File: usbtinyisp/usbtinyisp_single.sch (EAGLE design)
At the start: 23 parts, among them IC1 ATTINY2313-20P, IC2 74LVX125D, Q1 12000

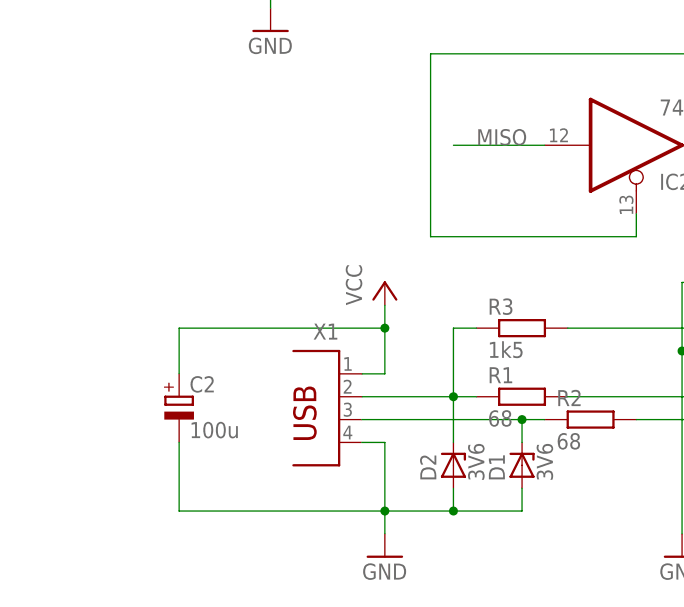
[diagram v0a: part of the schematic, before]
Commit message: add fuse and diode and route again the whole board
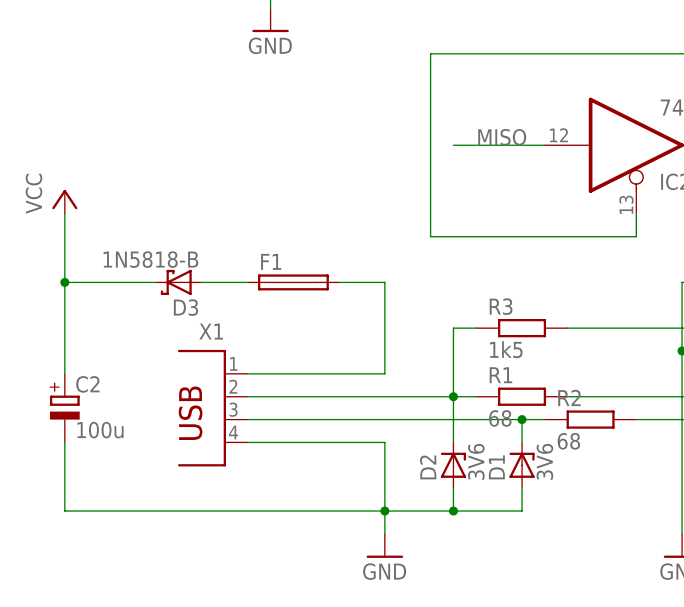
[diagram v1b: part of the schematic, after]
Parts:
- added D3: 1N5818-B, diode:1N5817-B
- added F1: (no value), n39:PTC-FUSE-LP60-050
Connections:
- new net N$14: D3.A, F1.1
- new net VBUS: F1.2, X1.1
- net VCC: now also D3.C; no longer X1.1
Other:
- moved on the sheet: C2, X1
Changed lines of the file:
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@@
 <part name="C4" library="rcl" deviceset="C-EU" device="C1206" value="22p"/>
 <part name="C5" library="rcl" deviceset="C-EU" device="C0805" value="100n"/>
+<part name="F1" library="n39" deviceset="PTC-FUSE" device="-LP60-050"/>
+<part name="D3" library="diode" deviceset="1N581*" device="" technology="7-B" value="1N5818-B"/>
 </parts>
 <sheets>
@@
 <instance part="JP3" gate="G$1" x="20.32" y="154.94" rot="MR180"/>
 <instance part="C1" gate="G$1" x="152.4" y="86.36"/>
-<instance part="P+1" gate="VCC" x="25.4" y="91.44"/>
+<instance part="P+1" gate="VCC" x="-10.16" y="101.6"/>
 <instance part="LED1" gate="G$1" x="66.04" y="91.44" rot="R270"/>
 <instance part="R6" gate="G$1" x="76.2" y="91.44"/>
@@
 <instance part="LED2" gate="G$1" x="66.04" y="83.82" rot="R270"/>
 <instance part="JP1" gate="1" x="22.86" y="134.62" rot="MR180"/>
-<instance part="X1" gate="G$1" x="20.32" y="76.2" rot="MR0"/>
+<instance part="X1" gate="G$1" x="7.62" y="76.2" rot="MR0"/>
 <instance part="IC2" gate="B" x="114.3" y="129.54" rot="R180"/>
 <instance part="IC2" gate="A" x="114.3" y="147.32" rot="R180"/>
@@
 <instance part="IC2" gate="D" x="53.34" y="106.68" rot="MR180"/>
 <instance part="IC2" gate="P" x="55.88" y="134.62"/>
-<instance part="C2" gate="G$1" x="2.54" y="78.74"/>
+<instance part="C2" gate="G$1" x="-10.16" y="78.74"/>
 <instance part="Q1" gate="G$1" x="165.1" y="99.06" rot="R90"/>
 <instance part="C3" gate="G$1" x="170.18" y="104.14" rot="R90"/>
 <instance part="C4" gate="G$1" x="170.18" y="93.98" rot="R90"/>
 <instance part="C5" gate="G$1" x="45.72" y="134.62"/>
+<instance part="F1" gate="G$1" x="15.24" y="91.44"/>
+<instance part="D3" gate="G$1" x="2.54" y="91.44" rot="R180"/>
 </instances>
 <busses>
@@
 <net name="N$1" class="0">
 <segment>
-<wire x1="22.86" y1="78.74" x2="33.02" y2="78.74" width="0.1524" layer="91"/>
+<wire x1="10.16" y1="78.74" x2="33.02" y2="78.74" width="0.1524" layer="91"/>
 <wire x1="33.02" y1="78.74" x2="35.56" y2="78.74" width="0.1524" layer="91"/>
 <wire x1="35.56" y1="86.36" x2="33.02" y2="86.36" width="0.1524" layer="91"/>
@@
 <net name="N$2" class="0">
 <segment>
-<wire x1="22.86" y1="76.2" x2="40.64" y2="76.2" width="0.1524" layer="91"/>
+<wire x1="10.16" y1="76.2" x2="40.64" y2="76.2" width="0.1524" layer="91"/>
 <wire x1="43.18" y1="76.2" x2="40.64" y2="76.2" width="0.1524" layer="91"/>
 <wire x1="40.64" y1="76.2" x2="40.64" y2="73.66" width="0.1524" layer="91"/>
@@
 </segment>
 <segment>
-<wire x1="25.4" y1="88.9" x2="25.4" y2="86.36" width="0.1524" layer="91"/>
-<wire x1="25.4" y1="86.36" x2="25.4" y2="81.28" width="0.1524" layer="91"/>
-<wire x1="25.4" y1="81.28" x2="22.86" y2="81.28" width="0.1524" layer="91"/>
-<wire x1="25.4" y1="86.36" x2="2.54" y2="86.36" width="0.1524" layer="91"/>
-<wire x1="2.54" y1="86.36" x2="2.54" y2="81.28" width="0.1524" layer="91"/>
-<junction x="25.4" y="86.36"/>
+<wire x1="-10.16" y1="99.06" x2="-10.16" y2="91.44" width="0.1524" layer="91"/>
+<pinref part="C2" gate="G$1" pin="+"/>
 <pinref part="P+1" gate="VCC" pin="VCC"/>
-<pinref part="X1" gate="G$1" pin="1"/>
-<pinref part="C2" gate="G$1" pin="+"/>
+<pinref part="D3" gate="G$1" pin="C"/>
+<wire x1="-10.16" y1="91.44" x2="-10.16" y2="81.28" width="0.1524" layer="91"/>
+<wire x1="0" y1="91.44" x2="-10.16" y2="91.44" width="0.1524" layer="91"/>
+<junction x="-10.16" y="91.44"/>
 </segment>
 </net>
@@
 <segment>
 <wire x1="25.4" y1="66.04" x2="25.4" y2="73.66" width="0.1524" layer="91"/>
-<wire x1="25.4" y1="73.66" x2="22.86" y2="73.66" width="0.1524" layer="91"/>
+<wire x1="25.4" y1="73.66" x2="10.16" y2="73.66" width="0.1524" layer="91"/>
 <wire x1="25.4" y1="66.04" x2="33.02" y2="66.04" width="0.1524" layer="91"/>
 <wire x1="33.02" y1="68.58" x2="33.02" y2="66.04" width="0.1524" layer="91"/>
@@
 <wire x1="40.64" y1="66.04" x2="40.64" y2="68.58" width="0.1524" layer="91"/>
 <wire x1="25.4" y1="63.5" x2="25.4" y2="66.04" width="0.1524" layer="91"/>
-<wire x1="25.4" y1="66.04" x2="2.54" y2="66.04" width="0.1524" layer="91"/>
-<wire x1="2.54" y1="66.04" x2="2.54" y2="73.66" width="0.1524" layer="91"/>
+<wire x1="25.4" y1="66.04" x2="-10.16" y2="66.04" width="0.1524" layer="91"/>
+<wire x1="-10.16" y1="66.04" x2="-10.16" y2="73.66" width="0.1524" layer="91"/>
 <pinref part="GND1" gate="1" pin="GND"/>
 <pinref part="D2" gate="G$1" pin="A"/>
@@
 </segment>
 </net>
+<net name="VBUS" class="1">
+<segment>
+<pinref part="X1" gate="G$1" pin="1"/>
+<wire x1="10.16" y1="81.28" x2="25.4" y2="81.28" width="0.1524" layer="91"/>
+<wire x1="25.4" y1="81.28" x2="25.4" y2="91.44" width="0.1524" layer="91"/>
+<pinref part="F1" gate="G$1" pin="2"/>
+<wire x1="25.4" y1="91.44" x2="20.32" y2="91.44" width="0.1524" layer="91"/>
+</segment>
+</net>
+<net name="N$14" class="1">
+<segment>
+<pinref part="F1" gate="G$1" pin="1"/>
+<pinref part="D3" gate="G$1" pin="A"/>
+<wire x1="10.16" y1="91.44" x2="5.08" y2="91.44" width="0.1524" layer="91"/>
+</segment>
+</net>
